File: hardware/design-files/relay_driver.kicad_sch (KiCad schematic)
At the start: 10 parts, among them J3 LOAD_OUT, K1 SRD-05VDC-SL-C, Q1 BC547B, U3 PC817

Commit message: feat(hardware): update KiCad schematics with component symbols and layout refinements
- Add ADS1115 16-bit I2C ADC symbol to CT sensor schematic
- Add AudioJack2 connector symbol for analog signal input
- Update ESP32 module schematic with refined pin configurations
- Update power supply schematic with improved component placement
- Update relay driver schematic with optimized routing
- Refine PCB layout in gateway.kicad_pcb with better trace routing
- Update project settings in gateway.kicad_pro for design rule compliance
- Add project rules configuration in gateway.kicad_prl for manufacturing constraints
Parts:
- removed D4: 1N4148, Diode_SMD:D_SOD-323, symbol Device:D
- removed D5: P6KE250CA, Diode_THT:D_DO-201_P15.24mm_Horizontal, symbol Device:D_TVS_bidirectional
- removed D6: LED_Green, LED_SMD:LED_0805_2012Metric, symbol Device:LED
- removed J3: LOAD_OUT, TerminalBlock:TerminalBlock_bornier-3_P5.08mm, symbol Connector:Screw_Terminal_01x03
- removed K1: SRD-05VDC-SL-C, Relay_THT:Relay_SPDT_SANYOU_SRD_Series_Form_C, symbol Relay:SANYOU_SRD_Form_C
- removed Q1: BC547B, Package_TO_SOT_THT:TO-92_Inline, symbol Transistor_BJT:BC547
- removed R5: 330R, Resistor_SMD:R_0805_2012Metric, symbol Device:R
- removed R6: 1K, Resistor_SMD:R_0805_2012Metric, symbol Device:R
- removed R7: 470R, Resistor_SMD:R_0805_2012Metric, symbol Device:R
- removed U3: PC817, Package_DIP:DIP-4_W7.62mm, symbol Isolator:PC817
- added K1: Screw_Terminal_01x04, Connector_PinHeader_2.54mm:PinHeader_1x02_P2.54mm_Vertical, symbol Connector:Screw_Terminal_01x04
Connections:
- net GND: now also K1.2 (Pin_2)
- net RELAY_CMD: now also K1.1 (Pin_1)
- new net +3.3V: K1.3 (Pin_3)
- new net +5V: K1.4 (Pin_4)
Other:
- note added: "GND"
- note added: "IN"
- note added: "JD-VCC"
- note added: "VCC"

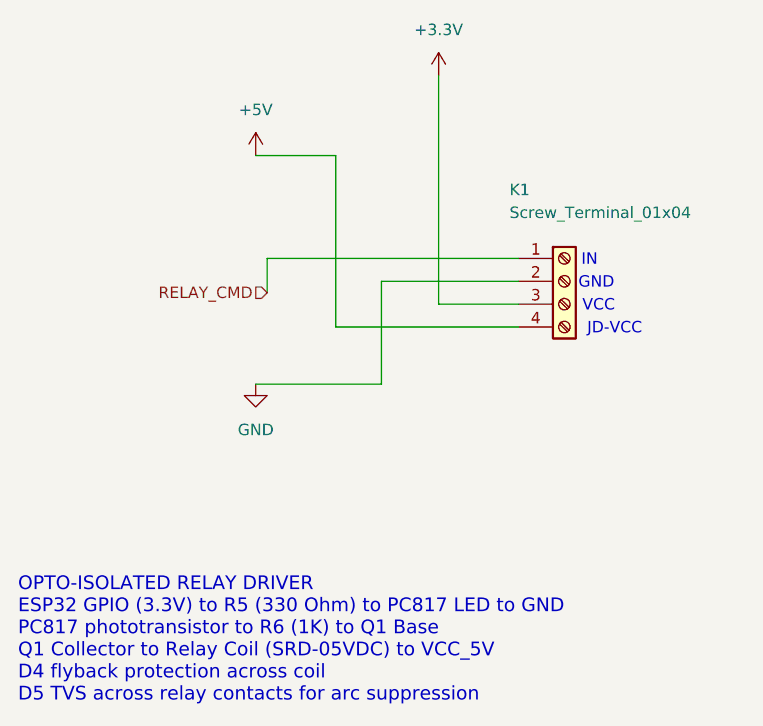
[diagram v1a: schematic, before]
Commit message: feat(hardware): update PCB layout and component footprints
- Reposition ADS1115 ADC module on PCB (moved from 84.35,28 to 60.5,49.35 with 180° rotation)
- Update CT sensor connector footprint from PinHeader to 3.5mm audio jack (Switronic ST-005-G)
- Correct ESP32 module connector footprint from 1x02 to 1x06 pin header
- Regenerate component UUIDs and silk screen coordinates to reflect new placements
- Optimize PCB layout for improved signal routing and component accessibility
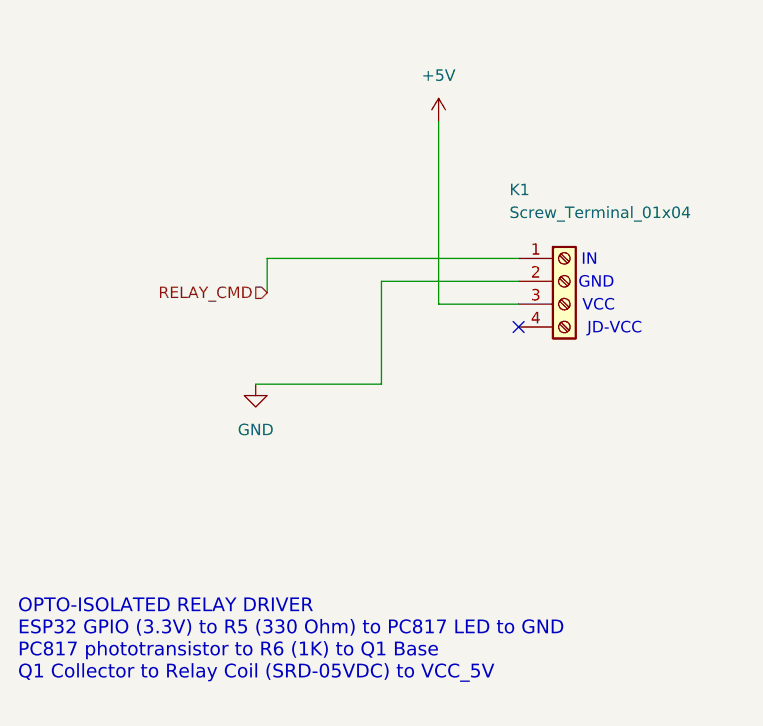
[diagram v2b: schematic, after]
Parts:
- K1: footprint Connector_PinHeader_2.54mm:PinHeader_1x02_P2.54mm_Vertical -> Connector_PinHeader_2.54mm:PinHeader_1x04_P2.54mm_Vertical
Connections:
- net +3.3V is gone; now on net +5V: K1.3 (Pin_3)
- net +5V: no longer K1.4 (Pin_4)
- no-connect marks 0 -> 1
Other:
- note added: "OPTO-ISOLATED RELAY DRIVER ESP32 GPIO (3.3V) to R5 (330 Ohm) to PC817 LED to GND PC817 phototransistor to R6 (1K) to Q1 Base Q1 Collector to Relay Coil (SRD-05VDC) to VCC_5V"
- note removed: "OPTO-ISOLATED RELAY DRIVER ESP32 GPIO (3.3V) to R5 (330 Ohm) to PC817 LED to GND PC817 phototransistor to R6 (1K) to Q1 Base Q1 Collector to Relay Coil (SRD-05VDC) to VCC_5V D4 flyback protection across coil D5 TVS across relay contacts for arc suppression"
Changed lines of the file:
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@@
 		)
 	)
-	(text "OPTO-ISOLATED RELAY DRIVER\nESP32 GPIO (3.3V) to R5 (330 Ohm) to PC817 LED to GND\nPC817 phototransistor to R6 (1K) to Q1 Base\nQ1 Collector to Relay Coil (SRD-05VDC) to VCC_5V\nD4 flyback protection across coil\nD5 TVS across relay contacts for arc suppression"
+	(text "OPTO-ISOLATED RELAY DRIVER\nESP32 GPIO (3.3V) to R5 (330 Ohm) to PC817 LED to GND\nPC817 phototransistor to R6 (1K) to Q1 Base\nQ1 Collector to Relay Coil (SRD-05VDC) to VCC_5V"
 		(exclude_from_sim no)
 		(at 30.734 104.648 0)
@@
 		)
 	)
+	(no_connect
+		(at 86.36 69.85)
+	)
 	(wire
 		(pts
@@
 	(wire
 		(pts
-			(xy 66.04 69.85) (xy 86.36 69.85)
-		)
-		(stroke
-			(width 0)
-			(type default)
-		)
-	)
-	(wire
-		(pts
 			(xy 71.12 76.2) (xy 71.12 64.77)
 		)
@@
 	(wire
 		(pts
-			(xy 66.04 50.8) (xy 66.04 69.85)
-		)
-		(stroke
-			(width 0)
-			(type default)
-		)
-	)
-	(wire
-		(pts
-			(xy 57.15 50.8) (xy 66.04 50.8)
-		)
-		(stroke
-			(width 0)
-			(type default)
-		)
-	)
-	(wire
-		(pts
 			(xy 58.42 62.23) (xy 86.36 62.23)
 		)
@@
 	(wire
 		(pts
-			(xy 77.47 41.91) (xy 77.47 67.31)
+			(xy 77.47 46.99) (xy 77.47 67.31)
 		)
 		(stroke
@@
 	(symbol
 		(lib_id "power:+5V")
-		(at 57.15 50.8 0)
+		(at 77.47 46.99 0)
 		(unit 1)
 		(body_style 1)
@@
 		(fields_autoplaced yes)
 		(property "Reference" "#PWR08"
-			(at 57.15 54.61 0)
+			(at 77.47 50.8 0)
 			(hide yes)
 			(show_name no)
@@
 		)
 		(property "Value" "+5V"
-			(at 57.15 45.72 0)
+			(at 77.47 41.91 0)
 			(show_name no)
 			(do_not_autoplace no)
@@
 		)
 		(property "Footprint" ""
-			(at 57.15 50.8 0)
+			(at 77.47 46.99 0)
 			(hide yes)
 			(show_name no)
@@
 		)
 		(property "Datasheet" ""
-			(at 57.15 50.8 0)
+			(at 77.47 46.99 0)
 			(hide yes)
 			(show_name no)
@@
 		)
 		(property "Description" "Power symbol creates a global label with name \"+5V\""
-			(at 57.15 50.8 0)
+			(at 77.47 46.99 0)
 			(hide yes)
 			(show_name no)
@@
 			)
 		)
-		(property "Footprint" "Connector_PinHeader_2.54mm:PinHeader_1x02_P2.54mm_Vertical"
+		(property "Footprint" "Connector_PinHeader_2.54mm:PinHeader_1x04_P2.54mm_Vertical"
 			(at 91.44 64.77 0)
 			(hide yes)
@@
 					(unit 1)
 				)
-			)
-		)
-	)
-	(symbol
-		(lib_id "power:+3.3V")
-		(at 77.47 41.91 0)
-		(unit 1)
-		(body_style 1)
-		(exclude_from_sim no)
-		(in_bom yes)
-		(on_board yes)
-		(in_pos_files yes)
-		(dnp no)
-		(fields_autoplaced yes)
-		(property "Reference" "#PWR01"
-			(at 77.47 45.72 0)
-			(hide yes)
-			(show_name no)
-			(do_not_autoplace no)
-			(effects
-				(font
-					(size 1.27 1.27)
-				)
-			)
-		)
-		(property "Value" "+3.3V"
-			(at 77.47 36.83 0)
-			(show_name no)
-			(do_not_autoplace no)
-			(effects
-				(font
-					(size 1.27 1.27)
-				)
-			)
-		)
-		(property "Footprint" ""
-			(at 77.47 41.91 0)
-			(hide yes)
-			(show_name no)
-			(do_not_autoplace no)
-			(effects
-				(font
-					(size 1.27 1.27)
-				)
-			)
-		)
-		(property "Datasheet" ""
-			(at 77.47 41.91 0)
-			(hide yes)
-			(show_name no)
-			(do_not_autoplace no)
-			(effects
-				(font
-					(size 1.27 1.27)
-				)
-			)
-		)
-		(property "Description" "Power symbol creates a global label with name \"+3.3V\""
-			(at 77.47 41.91 0)
-			(hide yes)
-			(show_name no)
-			(do_not_autoplace no)
-			(effects
-				(font
-					(size 1.27 1.27)
-				)
-			)
-		)
-		(pin "1"
-		)
-		(instances
-			(project "gateway"
-				(path "/e63e39d7-6ac0-4ffd-8aa3-1841a4541b55/d3c4e5f6-7a8b-9c0d-1e2f-3a4b5c6d7e8f"
-					(reference "#PWR01")
-					(unit 1)
-				)
